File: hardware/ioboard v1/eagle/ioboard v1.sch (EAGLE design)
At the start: 5 parts, among them IC1 MCP23017SO, K1 61300611021, K2 613006143121, K3 691402910008, K4 691402910008

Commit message: Intermediate commit of ioboard.
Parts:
- added IC2: (no value), ic:ULN2803A
- added IC3, IC4: ACPL-244, ic:ACPL-244
- added LED1, LED2, LED3, LED4, LED5, LED6, LED7, LED8: (no value), led:LEDCHIPLED_1206
- added RN1, RN2, RN3, RN4: (no value), dp_devices:RESISTOR_ARRAY_4
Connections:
- new net GND: IC3.11, IC3.13, IC3.15, IC3.2, IC3.4, IC3.6, IC3.8, IC3.9, IC4.11, IC4.13, IC4.15, IC4.2, IC4.4, IC4.6, IC4.8, IC4.9
- new net IN_SHIELD0: IC1.GPA0, IC3.16, RN3A.1
- new net IN_SHIELD1: IC1.GPA1, IC3.14, RN3B.1
- new net IN_SHIELD2: IC1.GPA2, IC3.12, RN3C.1
- new net IN_SHIELD3: IC1.GPA3, IC3.10, RN3D.1
- new net IN_SHIELD4: IC1.GPA4, IC4.16, RN4A.1
- new net IN_SHIELD5: IC1.GPA5, IC4.14, RN4B.1
- new net IN_SHIELD6: IC1.GPA6, IC4.12, RN4C.1
- new net IN_SHIELD7: IC1.GPA7, IC4.10, RN4D.1
- new net N$1: IC1.GPB0, IC2.I1
- new net N$10: IC3.3, RN1B.2
- new net N$11: IC3.5, RN1C.2
- new net N$12: IC3.7, RN1D.2
- new net N$13: IC4.1, RN2A.2
- new net N$14: IC4.3, RN2B.2
- new net N$15: IC4.5, RN2C.2
- new net N$16: IC4.7, RN2D.2
- new net N$17: LED1.C, RN3A.2
- new net N$18: LED2.C, RN3B.2
- new net N$19: K1.6, K2.1
- new net N$2: IC1.GPB1, IC2.I2
- new net N$20: K1.5, K2.2
- new net N$21: K1.4, K2.3
- new net N$22: K1.3, K2.4
- new net N$23: K1.2, K2.5
- new net N$24: K1.1, K2.6
- new net N$29: LED3.C, RN3C.2
- new net N$3: IC1.GPB2, IC2.I3
- new net N$30: LED4.C, RN3D.2
- new net N$36: LED5.C, RN4A.2
- new net N$37: LED6.C, RN4B.2
- new net N$38: LED7.C, RN4C.2
- new net N$39: LED8.C, RN4D.2
- new net N$4: IC1.GPB3, IC2.I4
- new net N$5: IC1.GPB4, IC2.I5
- new net N$6: IC1.GPB5, IC2.I6
- new net N$7: IC1.GPB6, IC2.I7
- new net N$8: IC1.GPB7, IC2.I8
- new net N$9: IC3.1, RN1A.2
- new net OUT0: IC2.O1, K4.1, K4.16
- new net OUT1: IC2.O2, K4.15, K4.2
- new net OUT2: IC2.O3, K4.14, K4.3
- new net OUT3: IC2.O4, K4.13, K4.4
- new net OUT4: IC2.O5, K4.12, K4.5
- new net OUT5: IC2.O6, K4.11, K4.6
- new net OUT6: IC2.O7, K4.10, K4.7
- new net OUT7: IC2.O8, K4.8, K4.9
- new net VDD: IC1.VDD, LED1.A, LED2.A, LED3.A, LED4.A, LED5.A, LED6.A, LED7.A, LED8.A
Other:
- moved on the sheet: K1, K2, K3, K4

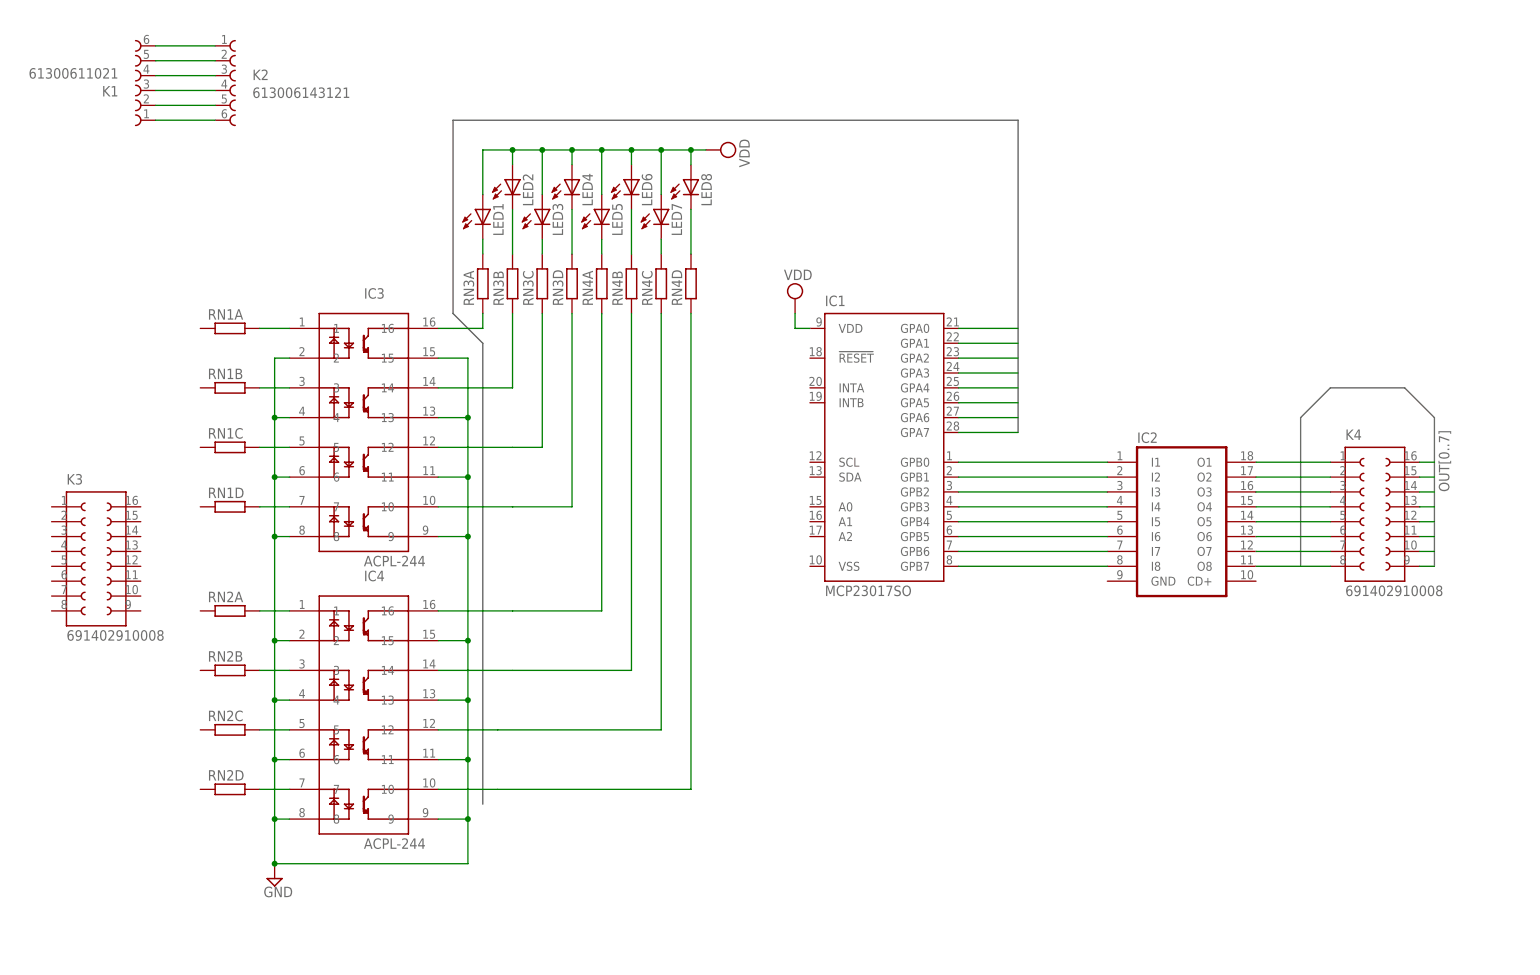
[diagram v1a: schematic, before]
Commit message: Updated IOboard with some more connectors and LEDs
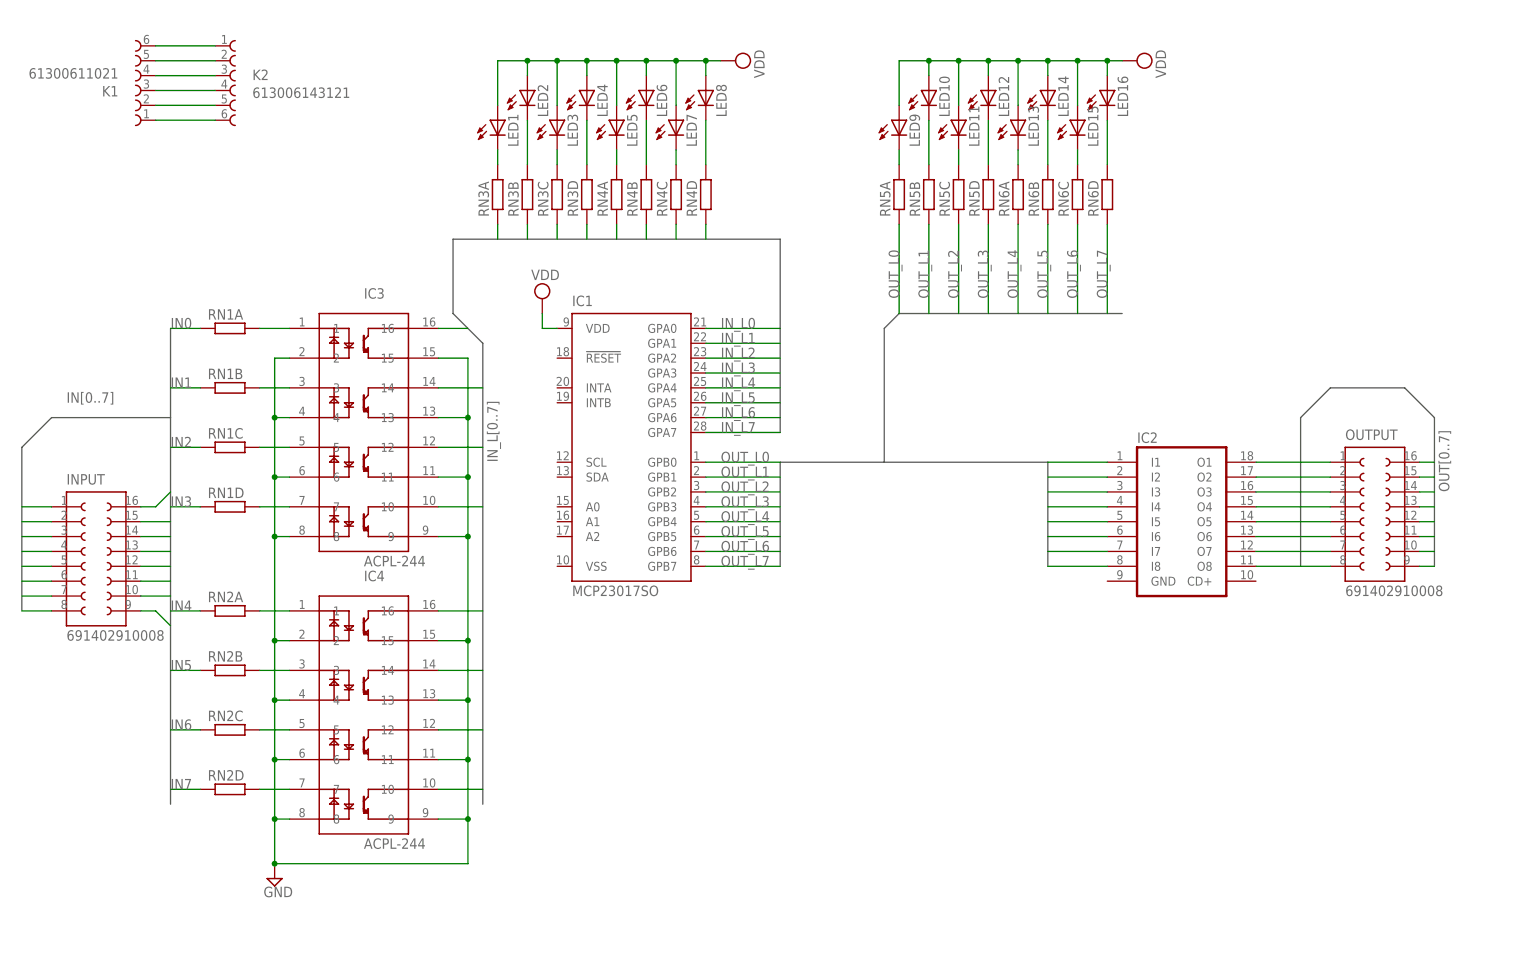
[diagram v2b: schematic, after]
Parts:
- added LED10, LED11, LED12, LED13, LED14, LED15, LED16, LED9: (no value), led:LEDCHIPLED_1206
- added RN5, RN6: (no value), dp_devices:RESISTOR_ARRAY_4
- renumbered K3 to INPUT, K4 to OUTPUT
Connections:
- net IN_SHIELD0 renamed IN_L0
- net IN_SHIELD1 renamed IN_L1
- net IN_SHIELD2 renamed IN_L2
- net IN_SHIELD3 renamed IN_L3
- net IN_SHIELD4 renamed IN_L4
- net IN_SHIELD5 renamed IN_L5
- net IN_SHIELD6 renamed IN_L6
- net IN_SHIELD7 renamed IN_L7
- removed net N$1: IC1.GPB0, IC2.I1
- removed net N$2: IC1.GPB1, IC2.I2
- removed net N$3: IC1.GPB2, IC2.I3
- removed net N$4: IC1.GPB3, IC2.I4
- removed net N$5: IC1.GPB4, IC2.I5
- removed net N$6: IC1.GPB5, IC2.I6
- removed net N$7: IC1.GPB6, IC2.I7
- removed net N$8: IC1.GPB7, IC2.I8
- new net IN0: INPUT.1, INPUT.16, RN1A.1
- new net IN1: INPUT.15, INPUT.2, RN1B.1
- new net IN2: INPUT.14, INPUT.3, RN1C.1
- new net IN3: INPUT.13, INPUT.4, RN1D.1
- new net IN4: INPUT.12, INPUT.5, RN2A.1
- new net IN5: INPUT.11, INPUT.6, RN2B.1
- new net IN6: INPUT.10, INPUT.7, INPUT.9, RN2C.1
- new net IN7: INPUT.8, RN2D.1
- new net N$25: LED9.C, RN5A.2
- new net N$26: LED10.C, RN5B.2
- new net N$27: LED11.C, RN5C.2
- new net N$28: LED12.C, RN5D.2
- new net N$31: LED13.C, RN6A.2
- new net N$32: LED14.C, RN6B.2
- new net N$33: LED15.C, RN6C.2
- new net N$34: LED16.C, RN6D.2
- new net OUT_L0: IC1.GPB0, IC2.I1, RN5A.1
- new net OUT_L1: IC1.GPB1, IC2.I2, RN5B.1
- new net OUT_L2: IC1.GPB2, IC2.I3, RN5C.1
- new net OUT_L3: IC1.GPB3, IC2.I4, RN5D.1
- new net OUT_L4: IC1.GPB4, IC2.I5, RN6A.1
- new net OUT_L5: IC1.GPB5, IC2.I6, RN6B.1
- new net OUT_L6: IC1.GPB6, IC2.I7, RN6C.1
- new net OUT_L7: IC1.GPB7, IC2.I8, RN6D.1
- net VDD: now also LED10.A, LED11.A, LED12.A, LED13.A, LED14.A, LED15.A, LED16.A, LED9.A
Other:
- moved on the sheet: IC1, LED1, LED2, LED3, LED4, LED5, LED6, LED7, LED8, RN3A, RN3B, RN3C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

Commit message: First board layout
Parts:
- added C1, C2: (no value), rcl:C-EUC0805
- added K4: 691214110003, Wuerth_Elektronik_eiCan_14_Terminal_Blocks_WR-TBL_2_0:691214110003
- added R1: (no value), rcl:R-EU_R0805
- added RN7: (no value), dp_devices:RESISTOR_ARRAY_4
- added SJ1: (no value), jumper:SJ
- added SW1: 418127270903, Eagle_Wuerth_Elektronik_Switch_Power_Elements:418127270903
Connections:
- removed net N$19: K1.6, K2.1
- removed net N$20: K1.5, K2.2
- removed net N$21: K1.4, K2.3
- removed net N$22: K1.3, K2.4
- removed net N$23: K1.2, K2.5
- removed net N$24: K1.1, K2.6
- new net !RST: C2.1, IC1.!RESET, RN7D.1, SJ1.1
- new net ADDR0: IC1.A0, RN7C.1, SW1.6
- new net ADDR1: IC1.A1, RN7B.1, SW1.5
- new net ADDR2: IC1.A2, RN7A.1, SW1.4
- new net AGND: IC3.2, IC3.4, IC3.6, IC3.8, IC4.2, IC4.4, IC4.6, IC4.8, K4.3
- new net INT: IC1.INTA, K1.1, K2.1, R1.2
- new net RST_EXT: K1.6, K2.6, SJ1.2
- new net SCL: IC1.SCL, K1.2, K2.2
- new net SDA: IC1.SDA, K1.5, K2.5
- new net V+: IC2.CD+, K4.1
- net GND: now also C1.2, C2.2, IC1.VSS, IC2.GND, K1.4, K2.4, K4.2, SW1.1, SW1.2, SW1.3; no longer IC3.2, IC3.4, IC3.6, IC3.8, IC4.2, IC4.4, IC4.6, IC4.8
- net IN6: no longer INPUT.9
- net IN7: now also INPUT.9
- net OUT0: now also IC2.O8, OUTPUT.15; no longer IC2.O1
- net OUT1: now also IC2.O7; no longer IC2.O2, OUTPUT.15
- net OUT2: now also IC2.O6; no longer IC2.O3
- net OUT3: now also IC2.O5; no longer IC2.O4
- net OUT4: now also IC2.O4; no longer IC2.O5
- net OUT5: now also IC2.O3; no longer IC2.O6
- net OUT6: now also IC2.O2; no longer IC2.O7
- net OUT7: now also IC2.O1; no longer IC2.O8
- net OUT_L0: now also IC2.I5, RN5D.1; no longer IC2.I1, RN5A.1
- net OUT_L1: now also IC2.I6, RN5C.1; no longer IC2.I2, RN5B.1
- net OUT_L2: now also IC2.I7, RN5B.1; no longer IC2.I3, RN5C.1
- net OUT_L3: now also IC2.I8, RN5A.1; no longer IC2.I4, RN5D.1
- net OUT_L4: now also IC2.I1, RN6D.1; no longer IC2.I5, RN6A.1
- net OUT_L5: now also IC2.I2, RN6C.1; no longer IC2.I6, RN6B.1
- net OUT_L6: now also IC2.I3, RN6B.1; no longer IC2.I7, RN6C.1
- net OUT_L7: now also IC2.I4, RN6A.1; no longer IC2.I8, RN6D.1
- net VDD: now also C1.1, K1.3, K2.3, R1.1, RN7A.2, RN7B.2, RN7C.2, RN7D.2

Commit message: Ordernumbers completed
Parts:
- C1, C2: MF (none) -> AVX; MPN (none) -> 08051A100JAT2A; OC_FARNELL (none) -> 499158
- IC1: MF (none) -> MICROCHIP; MPN (none) -> MCP23017-E/SO; OC_FARNELL (none) -> 1332087
- IC2: MF (none) -> TOSHIBA; MPN (none) -> ULN2803APG
- IC3, IC4: MF (none) -> AVAGO TECHNOLOGIES; MPN (none) -> ACPL-244-500E; OC_FARNELL (none) -> 1634755
- INPUT, K1, K2, LED1, LED10, LED11, LED12, LED13, LED14, LED15, LED16, LED2, LED3, LED4, LED5, LED6, LED7, LED8, LED9, OUTPUT, R1, RN1, RN2, RN3, RN4, RN5, RN6, RN7, SJ1, SW1: OC_FARNELL (none) -> unknown
- K4: MF (none) -> WURTH ELEKTRONIK; MPN (none) -> 691214110003; OC_FARNELL (none) -> 1841251
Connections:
- net OUT0: no longer OUTPUT.15
- net OUT1: now also OUTPUT.15
- net OUT_L0: now also IC2.I8; no longer IC2.I5
- net OUT_L1: now also IC2.I7; no longer IC2.I6
- net OUT_L2: now also IC2.I6; no longer IC2.I7
- net OUT_L3: now also IC2.I5; no longer IC2.I8
- net OUT_L4: now also IC2.I4; no longer IC2.I1
- net OUT_L5: now also IC2.I3; no longer IC2.I2
- net OUT_L6: now also IC2.I2; no longer IC2.I3
- net OUT_L7: now also IC2.I1; no longer IC2.I4
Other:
- moved on the sheet: K4
